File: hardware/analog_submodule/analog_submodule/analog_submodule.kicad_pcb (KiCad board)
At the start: 2 copper layers, 213 parts, among them J1 HVIN1, J10 HSADC in, J2 HVIN2, J3 CIN1, J4 CIN2, J5 LVIN+, J6 LVIN-, J7 RES_THERM, J8 AOUT, J9 MCU I/F, Q1 BSS138, Q2 BSS138, Q3 BSS138, Q4 BSS138, U1 AMS1117-5.0, U10 CD4051B, U100 LM6171D, U11 TL084, U12 TL084, U13 TLV9002IDR, U2 CD4051B, U3 CD4051B, U4 CD4051B, U5 CD4051B, U6 TLV9004IDR, U7 ADS131M02IPWR, U8 DAC101C081CIMK, U9 LM6171D, X1 ASV-xxxMHz

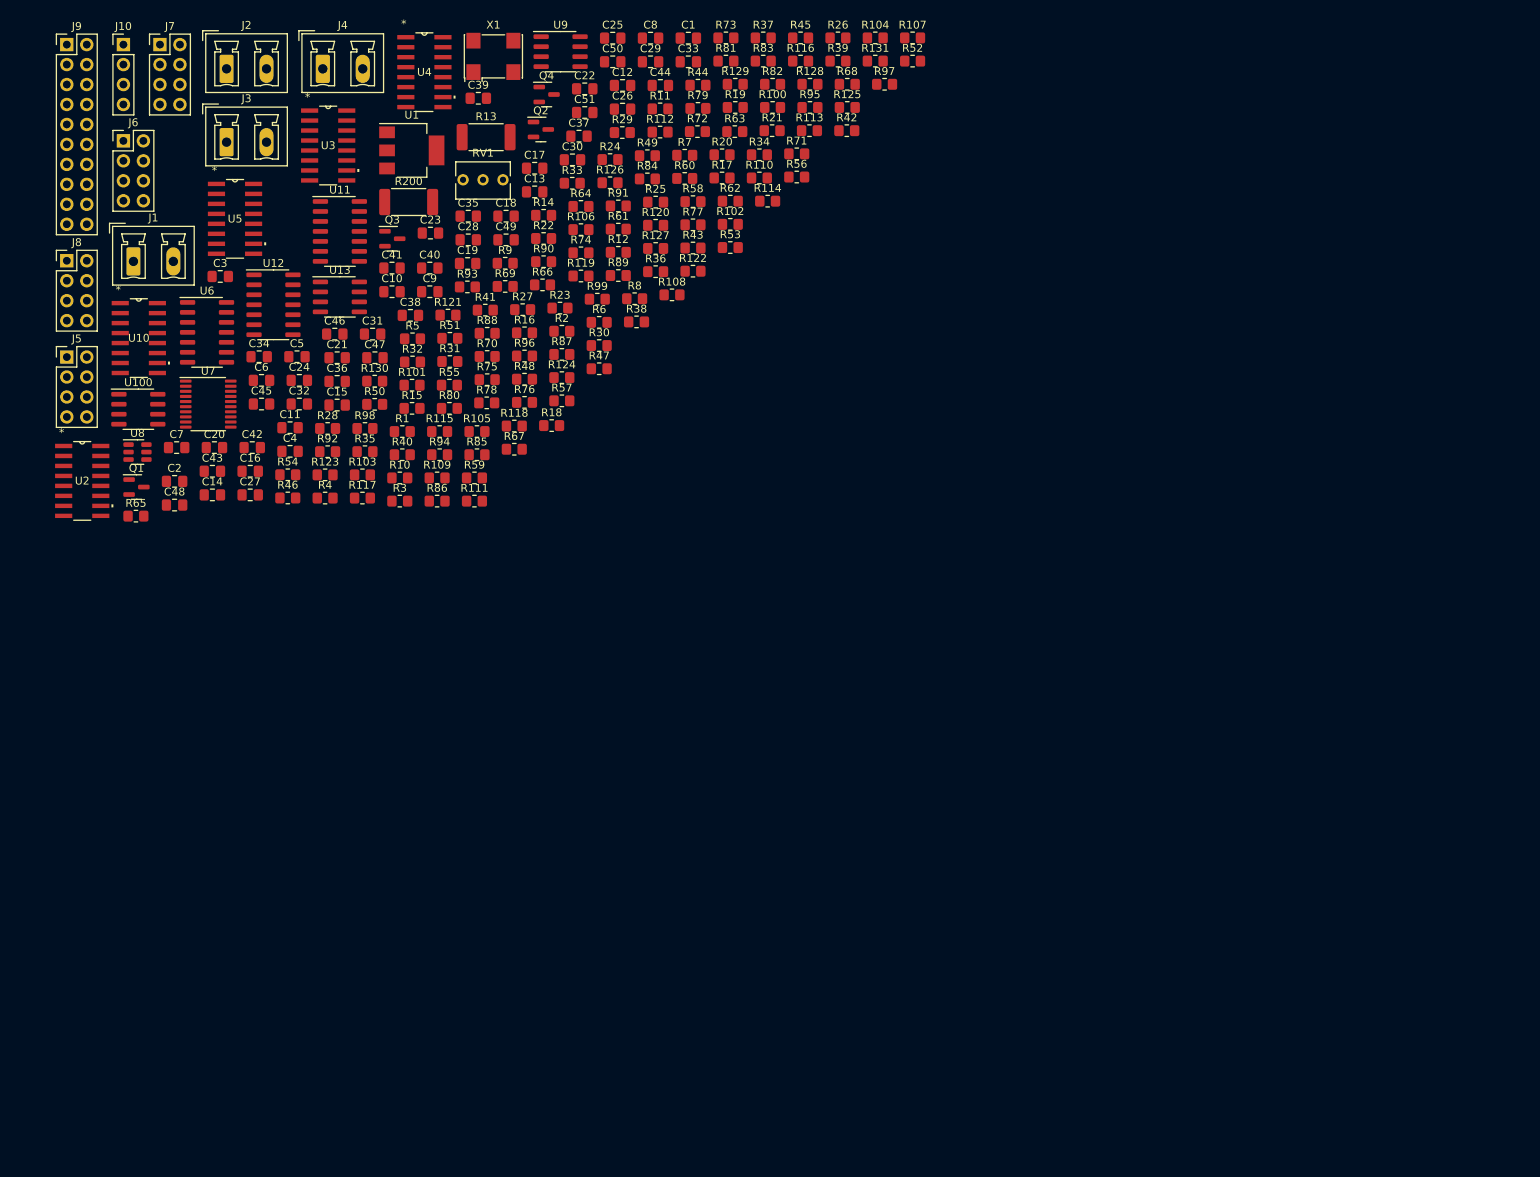
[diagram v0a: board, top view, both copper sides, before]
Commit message: Completed PCB design for analog submodule
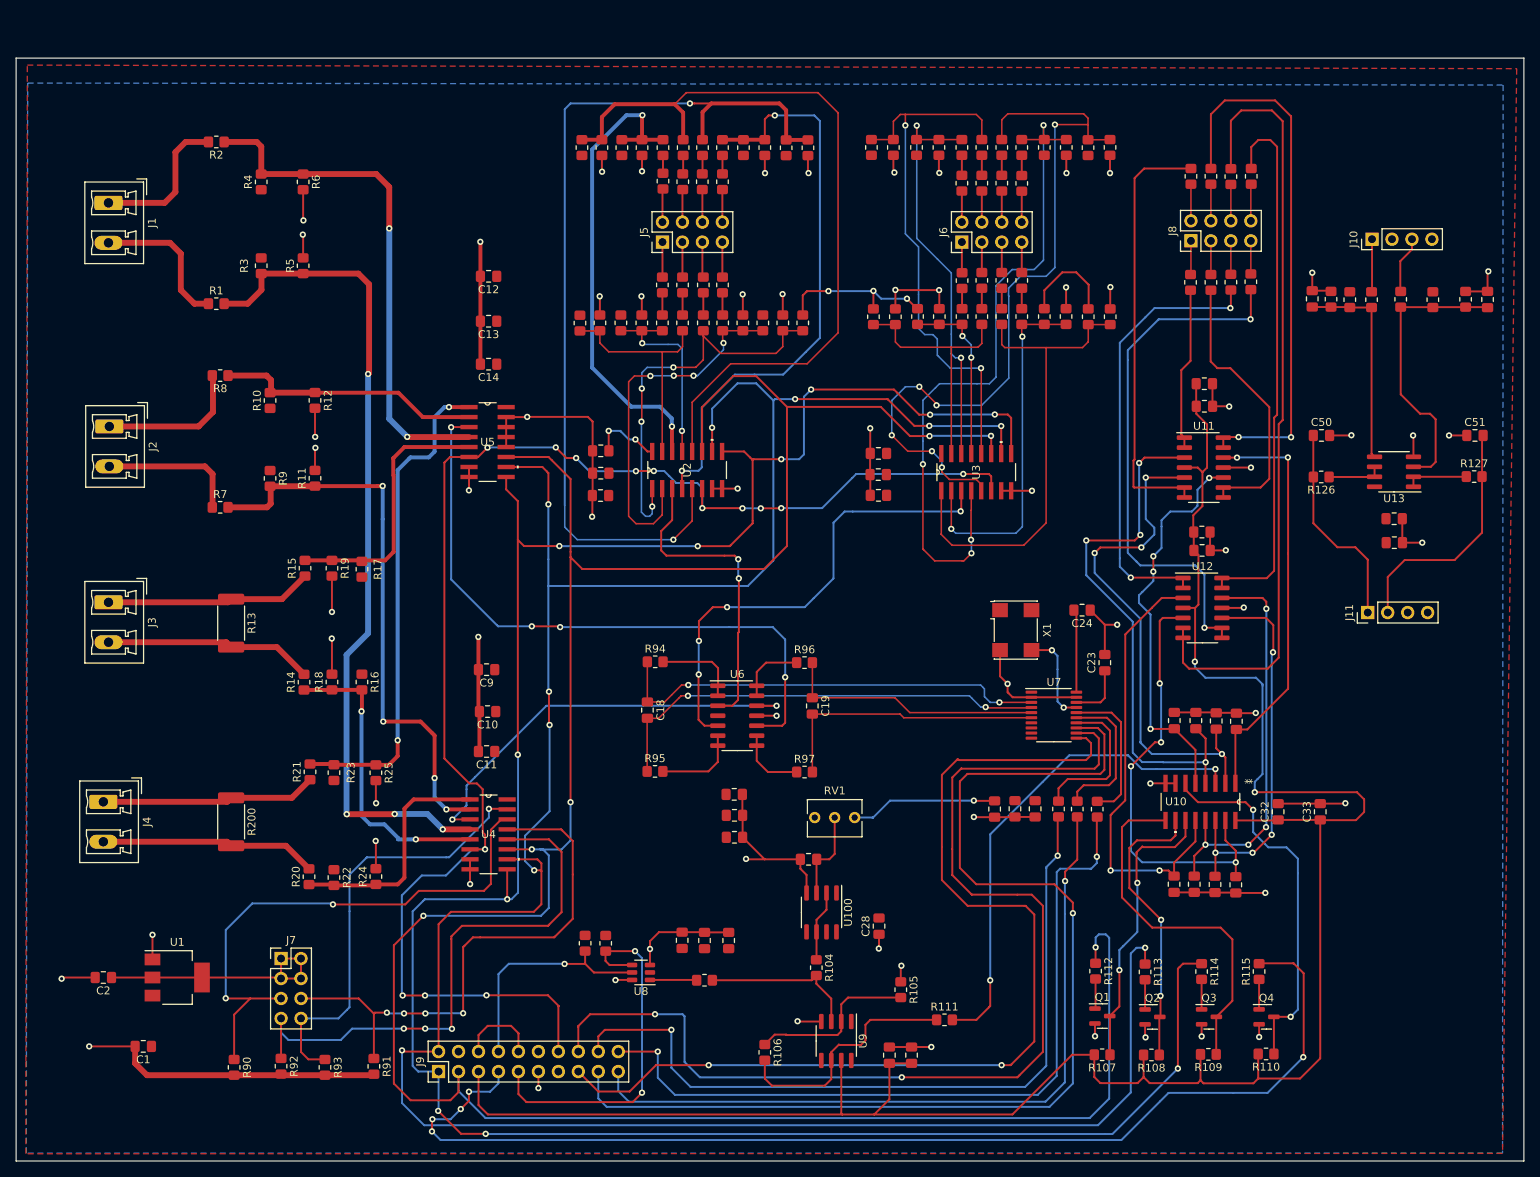
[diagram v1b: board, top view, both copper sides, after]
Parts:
- added J11: HSADC in, Connector_PinHeader_2.54mm:PinHeader_1x04_P2.54mm_Vertical, F.Cu at (193.8, 94.9)
- moved J10 160.8 mm to (194.3, 47.4), turned to 90 degrees
- moved C48 155.3 mm to (197.1, 86.0)
- moved Q4 148.8 mm to (180.9, 146.4)
- moved U10 147.4 mm to (172.5, 119.0), turned to -90 degrees
- moved C1 145.8 mm to (38.0, 150.1), turned to 180 degrees
- moved Q3 143.5 mm to (173.6, 146.4)
- moved J8 143.0 mm to (171.3, 47.6), turned to 90 degrees
- moved C47 141.7 mm to (209.0, 55.1), turned to 90 degrees
- moved Q1 140.1 mm to (160.0, 146.3)
- moved J9 138.9 mm to (75.5, 153.3), turned to 90 degrees
- moved Q2 137.1 mm to (166.4, 146.4)
- moved C34 136.6 mm to (171.7, 129.5), turned to -90 degrees
- moved U13 135.9 mm to (197.1, 77.0), turned to 180 degrees
- moved C32 134.9 mm to (182.3, 120.3), turned to 90 degrees
- moved R107 131.6 mm to (160.0, 151.2), turned to 180 degrees
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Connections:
- J8 pad 2: AOUT1+ -> AOUT0-
- J8 pad 3: AOUT2+ -> AOUT1+
- J8 pad 4: AOUT3+ -> AOUT1-
- J8 pad 5: AOUT3- -> AOUT2+
- J8 pad 7: AOUT1- -> AOUT3+
- J8 pad 8: AOUT0- -> AOUT3-
- J9 pad 12: HSADC1 -> GND
- J9 pad 13: HSADC0 -> GND
- Q2 pad 1: GND -> Net-(Q2-Pad1)
- Q3 pad 1: GND -> Net-(Q3-Pad1)
- R113 pad 2: GND -> Net-(Q2-Pad1)
- R114 pad 2: GND -> Net-(Q3-Pad1)
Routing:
- net GND: track 0.00 -> 372.5 mm, vias 0 -> 66
- net MUX2: track 0.00 -> 333.5 mm, vias 0 -> 6
- net MUX1: track 0.00 -> 327.8 mm, vias 0 -> 10
- net MUX0: track 0.00 -> 305.5 mm, vias 0 -> 11
- net 17V5: track 0.00 -> 275.4 mm, vias 0 -> 2
- net SDADC_DIS: track 0.00 -> 187.2 mm, vias 0 -> 14
- net DACEN: track 0.00 -> 146.6 mm, vias 0 -> 5
- net ADC_DRDY: track 0.00 -> 143.1 mm, vias 0 -> 1
- net ADC_CS: track 0.00 -> 141.0 mm, vias 0 -> 2
- net ADC_RST: track 0.00 -> 128.6 mm, vias 0 -> 2
- net LVCH6_P: track 0.00 -> 115.6 mm, vias 0 -> 2
- net HVCH1_P: track 0.00 -> 107.0 mm, vias 0 -> 4
- net Net-(R121-Pad1): track 0.00 -> 99.8 mm
- net LVCH4_P: track 0.00 -> 99.3 mm
- net LVCH6_N: track 0.00 -> 98.6 mm, vias 0 -> 6
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- added copper zone on F.Cu, net 3V3
- added copper zone on B.Cu, net GND
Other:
- board outline added: 191.8 x 140.3 mm
